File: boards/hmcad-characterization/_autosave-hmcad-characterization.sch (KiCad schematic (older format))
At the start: 58 parts, among them J1 BARREL, J10 SMA, J11 SMA, J12 CONN_INTEGRALSTICK_FPGA_HOST, J2 SMA, J3 SMA, J4 SMA, J5 SMA, J6 SMA, J7 SMA, J8 SMA, J9 SMA, U1 ASG2-D-X-A-1000.000MHZ, U2 SIT9122AI-2D3-33E625.000000T, U3 PI6C59S6005, U4 LT3042, U5 HMCAD1520, U6 LT3042

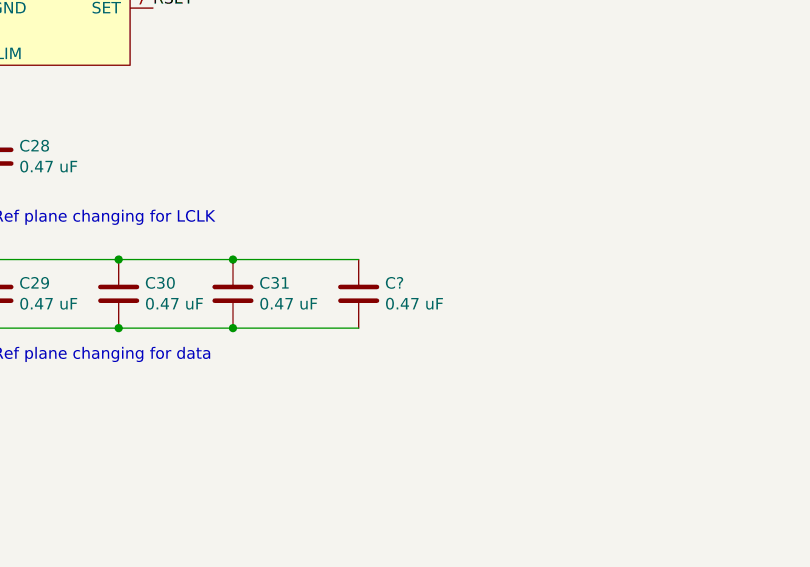
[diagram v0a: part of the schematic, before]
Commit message: Additional routing tweaks, added soldermask cutouts over RF traces
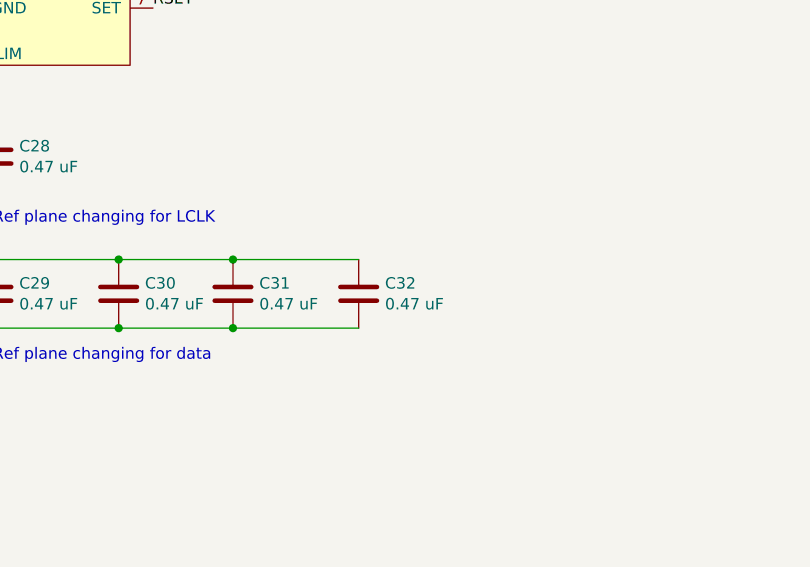
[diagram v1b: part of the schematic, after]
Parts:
- gave numbers to parts that had none: 1
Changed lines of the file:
@@
 Connection ~ 8750 5150
 $Comp
-L device:C C?
+L device:C C32
 U 1 1 5EF3F53B
 P 9800 5000
-F 0 "C?" H 9685 4954 50  0000 R CNN
+F 0 "C32" H 9685 4954 50  0000 R CNN
 F 1 "0.47 uF" H 9685 5045 50  0000 R CNN
 F 2 "azonenberg_pcb:EIA_0402_CAP_NOSILK" H 9838 4850 50  0001 C CNN
